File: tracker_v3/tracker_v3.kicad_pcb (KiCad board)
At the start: 2 copper layers, 72.5 x 22.1 mm, 37 parts, among them J1 USB_C_Receptacle_PowerOnly_6P, J2 P70-7000045, J3 P70-7000045, Q1 DMG9926UDM-7, U1 XIAO-ESP32-DIP, U2 LIS3DH, U3 DW01A, U4 INA226AIDGSR, U5 TP4056-42-ESOP8

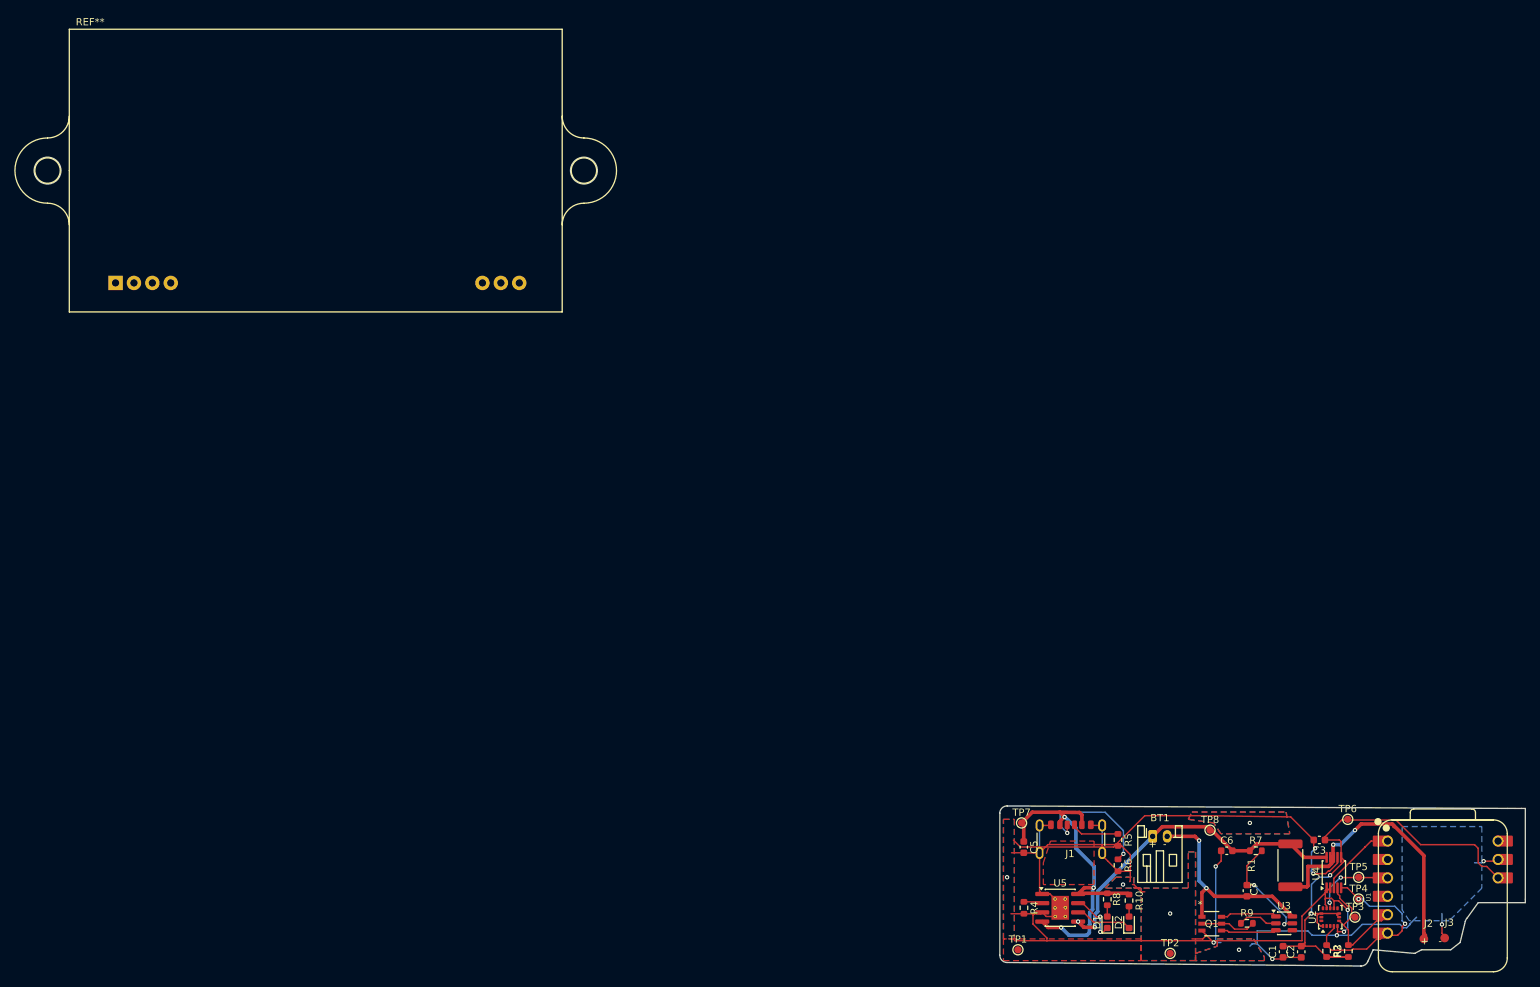
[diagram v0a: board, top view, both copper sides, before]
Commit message: the type c connector is pointing in the wrong direction
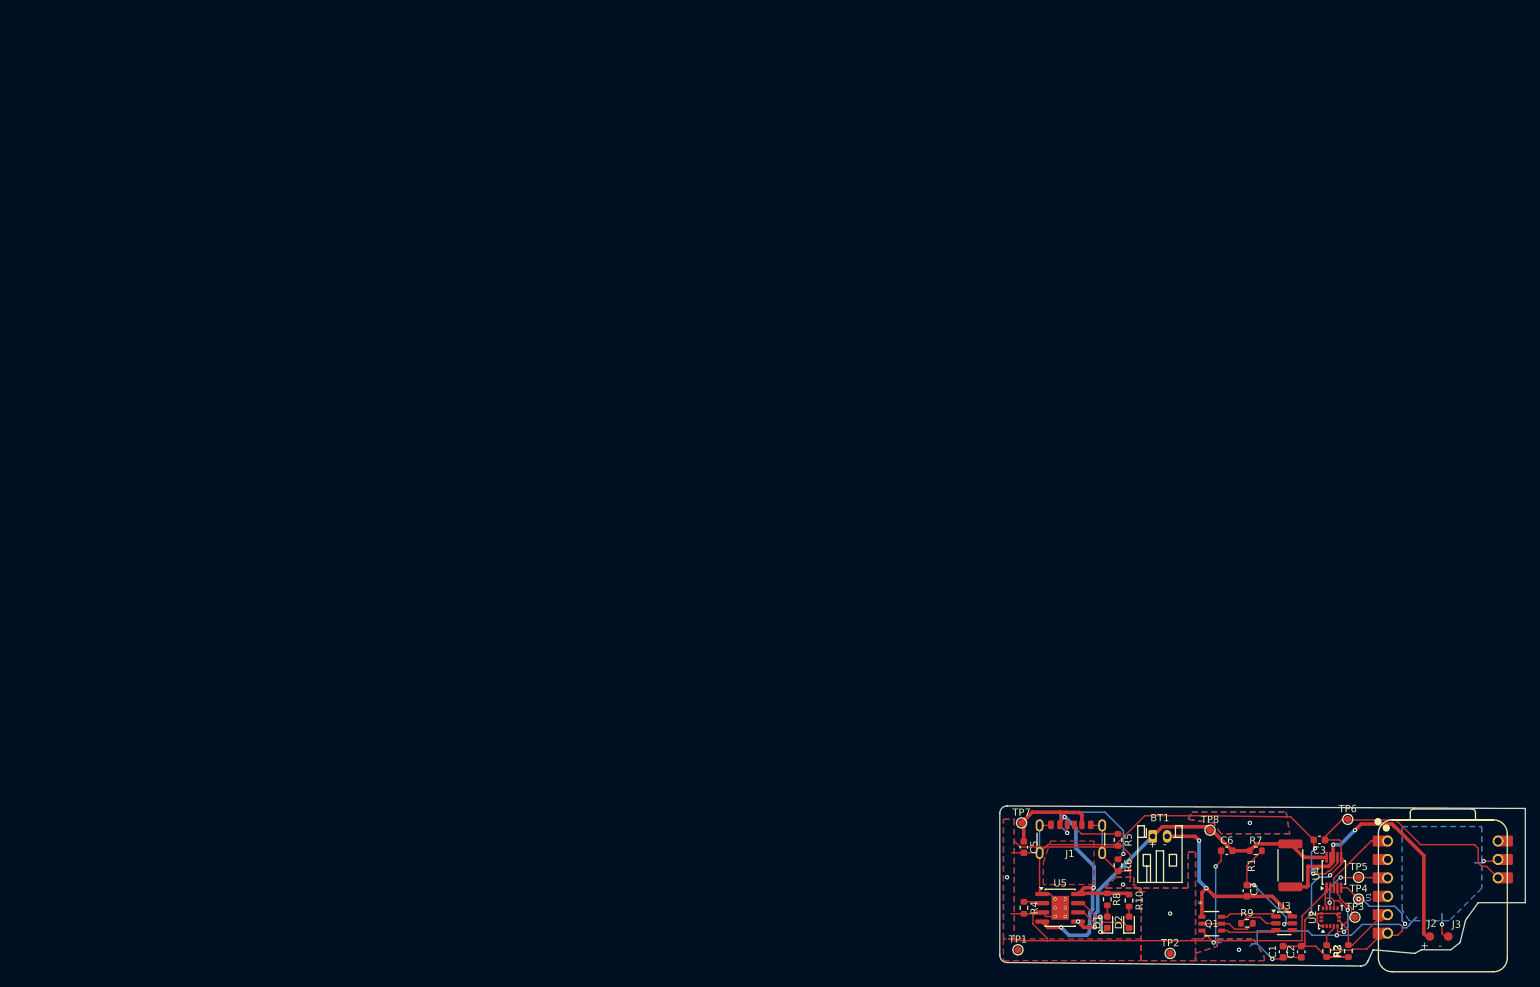
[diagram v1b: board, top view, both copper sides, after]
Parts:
- removed REF**: Reverb_BTDR-1H, Audio_Module:Reverb_BTDR-1H
- moved J3 0.53 mm to (183.0, 90.0)
- moved J2 0.50 mm to (181.0, 90.5)

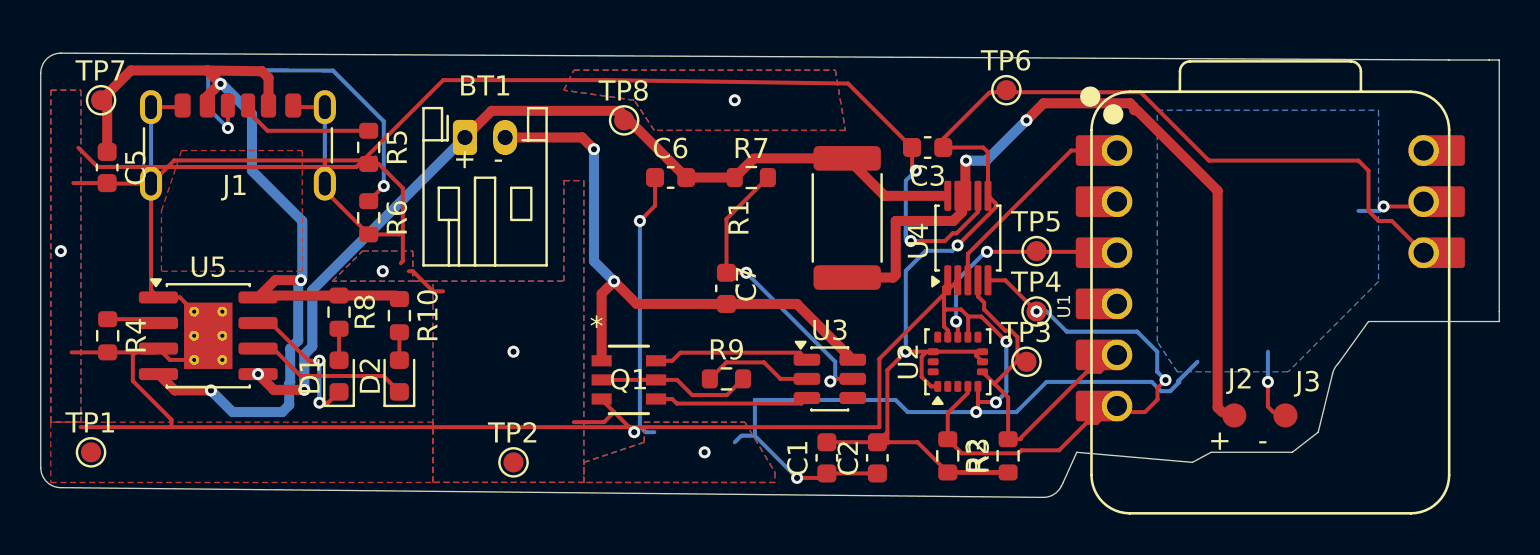
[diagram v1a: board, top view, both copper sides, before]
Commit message: added through holes
corrected the type-c charger, battery cable and corrected position of the pogo pins
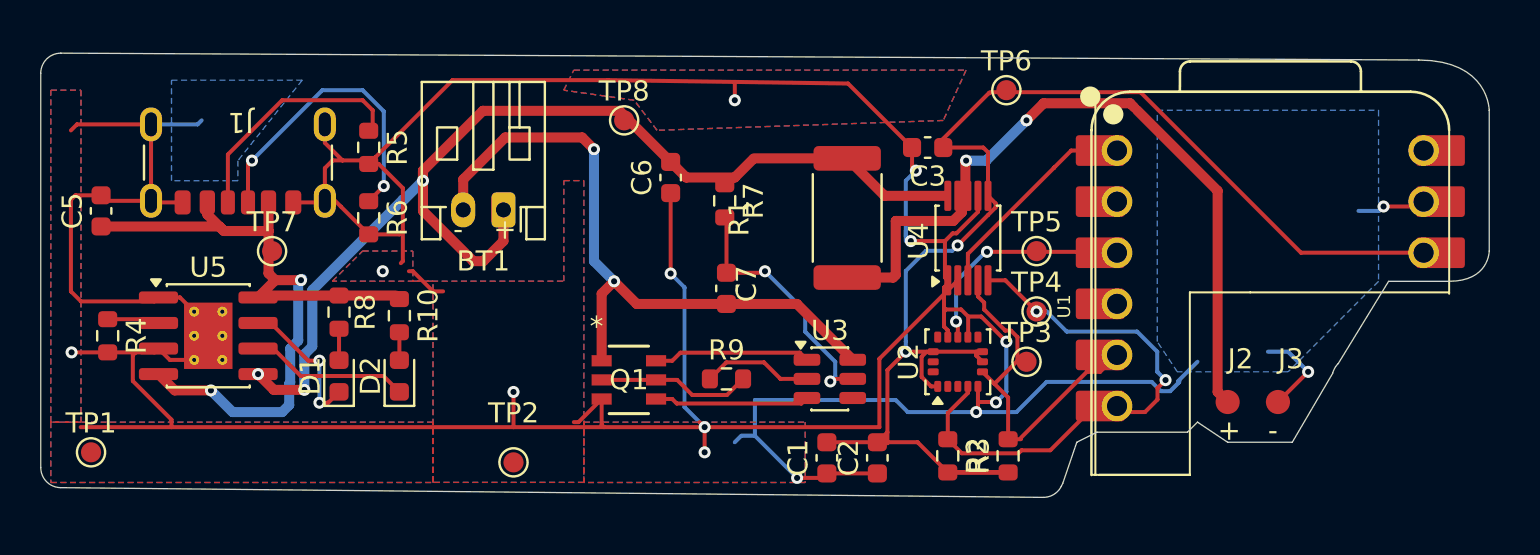
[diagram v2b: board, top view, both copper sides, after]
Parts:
- moved TP7 11.3 mm to (133.5, 82.0)
- moved BT1 4.08 mm to (145.0, 80.0), turned to 180 degrees
- moved C5 2.18 mm to (125.0, 80.0), turned to 90 degrees
- moved R7 1.76 mm to (156.0, 79.5), turned to -90 degrees
- moved J1 1.34 mm to (131.8, 76.5), turned to 180 degrees
- moved J2 1.00 mm to (181.0, 89.5)
- moved J3 0.71 mm to (183.5, 89.5)
- turned C6 to 90 degrees
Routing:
- net USB_VBUS: track 51.0 -> 37.6 mm, vias 3 -> 2
- net GND: track 233.5 -> 223.5 mm, vias 12 -> 15
- net /Charging_and_Battery/BAT+: track 45.9 -> 54.8 mm, vias 2 -> 3
- net Net-(J1-CC2): track 6.68 -> 12.0 mm
- net /Charging_and_Battery/BAT-: track 29.3 -> 33.8 mm
- net Net-(J1-CC1): track 18.2 -> 15.4 mm
- net Net-(U3-VCC): track 15.2 -> 13.0 mm
- net 3v3: track 69.8 -> 68.6 mm
- net SCL: track 27.7 -> 27.0 mm
- net /Shunt_Output: track 37.7 -> 37.2 mm
- net (no net): vias 3 -> 0
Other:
- board size 72.5 x 22.1 mm -> 72 x 22.1 mm

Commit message: v3.0 complete
the v3.0 has been added to cart for buying
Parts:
- moved C6 15.6 mm to (143.0, 90.0)
- moved R4 13.7 mm to (138.5, 90.0), turned to 0 degrees
- moved TP1 13.5 mm to (138.0, 92.5)
- moved R5 8.31 mm to (146.5, 75.5)
- moved R6 8.24 mm to (146.5, 79.5)
- moved U5 8.20 mm to (138.5, 85.9)
- moved J1 8.19 mm to (140.0, 76.9)
- moved C5 8.09 mm to (133.0, 81.2)
- moved TP8 7.76 mm to (158.5, 77.5)
- moved D1 7.73 mm to (144.5, 87.3)
- moved D2 7.73 mm to (147.5, 87.3)
- moved R10 7.73 mm to (147.5, 84.3)
- moved R8 7.73 mm to (144.5, 84.1)
- moved BT1 7.01 mm to (152.0, 79.5)
- moved TP2 6.02 mm to (151.5, 92.0)
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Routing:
- net GND: track 223.5 -> 153.3 mm, vias 15 -> 13
- net /Charging_and_Battery/BAT+: track 54.8 -> 35.4 mm, vias 3 -> 2
- net /Charging_and_Battery/BAT-: track 33.8 -> 21.9 mm, vias 2 -> 0
- net /Shunt_Output: track 37.2 -> 48.4 mm
- net Net-(J1-CC1): track 15.4 -> 6.92 mm, vias 2 -> 0
- net USB_VBUS: track 37.6 -> 29.2 mm, vias 2 -> 0
- net Net-(U5-PROG): track 2.60 -> 7.52 mm, vias 0 -> 2
- net 3v3: track 68.6 -> 64.9 mm
- net Net-(U3-VCC): track 13.0 -> 16.0 mm
- net Net-(J1-CC2): track 12.0 -> 9.58 mm
- net (no net): track 2.11 -> 0.00 mm
- net Net-(D2-K): track 8.17 -> 7.14 mm
- net SCL: track 27.0 -> 26.3 mm
- net SDA: track 17.6 -> 18.2 mm
- net Net-(D1-K): track 6.48 -> 5.88 mm
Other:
- board size 72 x 22.1 mm -> 62.5 x 22.1 mm
